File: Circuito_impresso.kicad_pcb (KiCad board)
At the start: 2 copper layers, 78.7 x 62.2 mm, 14 parts, among them J1 Extra_inputs, J2 MAX485M/left, J3 MAX485M/right, J4 RPI, Q1 TIP2955, U1 L7805

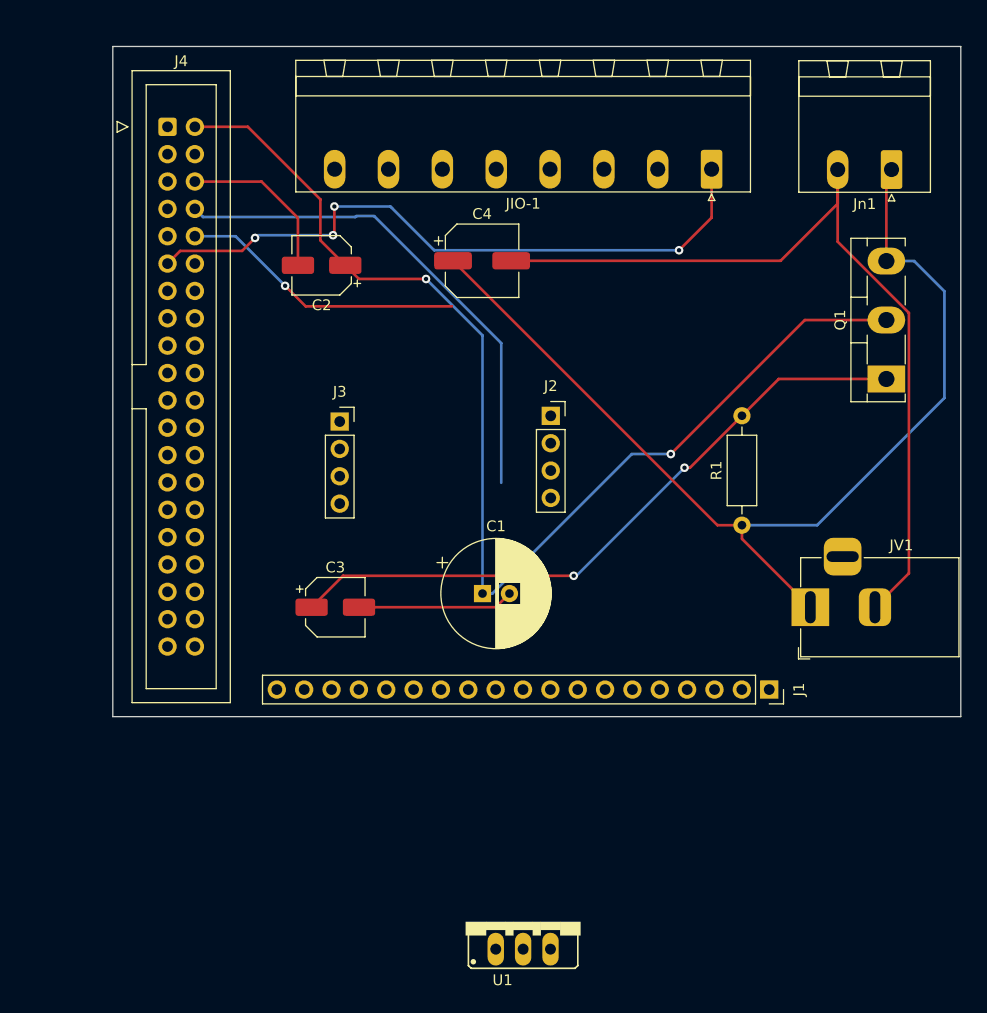
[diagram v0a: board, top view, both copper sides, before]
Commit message: Finalizes the preliminary design of the PCB
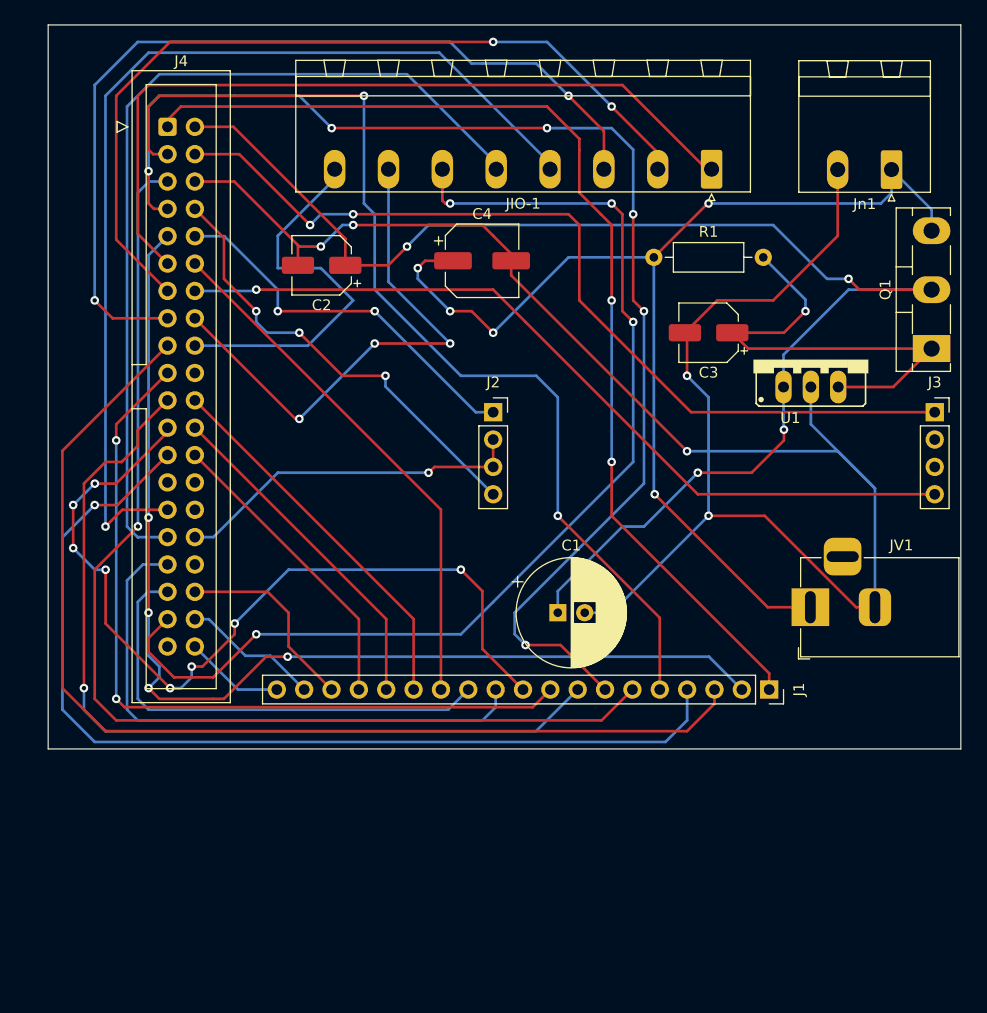
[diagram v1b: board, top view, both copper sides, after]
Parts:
- moved U1 58.6 mm to (171.5, 87.5)
- moved J3 55.3 mm to (183.0, 92.4)
- moved C3 43.0 mm to (162.0, 85.0), turned to 180 degrees
- moved R1 26.2 mm to (156.9, 78.0), turned to 0 degrees
- moved C1 7.21 mm to (148.0, 111.0)
- moved J2 5.36 mm to (142.0, 92.4)
- moved Q1 5.06 mm to (182.7, 86.5)
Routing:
- net Net-(J1-Pad7): track 0.00 -> 119.4 mm, vias 0 -> 6
- net Net-(J1-Pad6): track 0.00 -> 103.8 mm, vias 0 -> 1
- net Net-(J1-Pad2): track 0.00 -> 101.9 mm, vias 0 -> 4
- net Net-(J4-Pad37): track 0.00 -> 101.6 mm, vias 0 -> 4
- net Net-(J1-Pad3): track 0.00 -> 100.4 mm
- net Net-(J1-Pad1): track 0.00 -> 99.1 mm, vias 0 -> 2
- net Net-(J1-Pad5): track 0.00 -> 97.0 mm, vias 0 -> 2
- net Net-(J4-Pad29): track 0.00 -> 94.1 mm, vias 0 -> 1
- net Net-(J1-Pad4): track 0.00 -> 91.9 mm, vias 0 -> 1
- net Net-(J3-Pad1): track 0.00 -> 83.6 mm, vias 0 -> 2
- net Net-(J4-Pad15): track 0.00 -> 83.4 mm, vias 0 -> 2
- net Net-(J4-Pad31): track 0.00 -> 82.7 mm
- net Net-(J1-Pad8): track 0.00 -> 81.1 mm, vias 0 -> 1
- net Net-(J1-Pad10): track 0.00 -> 79.5 mm, vias 0 -> 8
- net Net-(J4-Pad13): track 0.00 -> 78.2 mm, vias 0 -> 2
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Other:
- board size 78.7 x 62.2 mm -> 84.7 x 67.2 mm

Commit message: updates to meet requirements; error correction
the width of the tracks is now 0.8 mm (considering the maximum circuit current of 5 amps, with a maximum increase of 40°C; the position of each terminal of the l7805 in the schematic has been corrected; the position of the L7 so that it heatsink does not collide with the TIP

The silkscreen must be done
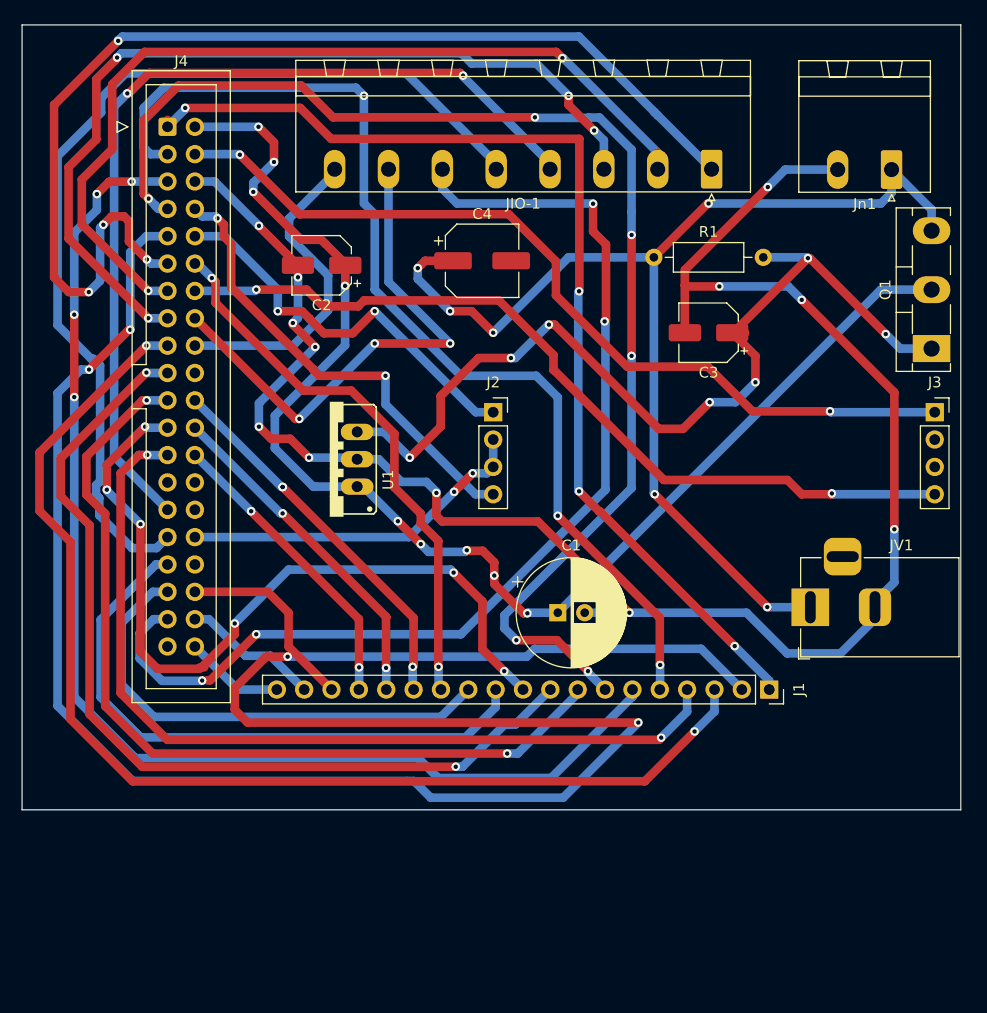
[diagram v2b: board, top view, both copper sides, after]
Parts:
- moved U1 45.6 mm to (126.8, 96.7), turned to 90 degrees
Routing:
- net Net-(J1-Pad2): track 101.9 -> 200.0 mm
- net Net-(C3-Pad1): track 43.5 -> 86.3 mm, vias 1 -> 7
- net Net-(J4-Pad11): track 73.7 -> 105.6 mm, vias 0 -> 4
- net Net-(J1-Pad9): track 73.5 -> 85.9 mm
- net Net-(J1-Pad6): track 103.8 -> 114.0 mm, vias 1 -> 4
- net Net-(J4-Pad31): track 82.7 -> 92.1 mm
- net Net-(J1-Pad4): track 91.9 -> 83.0 mm, vias 1 -> 2
- net Net-(J4-Pad29): track 94.1 -> 85.3 mm, vias 1 -> 2
- net Net-(J1-Pad3): track 100.4 -> 108.9 mm, vias 0 -> 2
- net Net-(C1-Pad1): track 132.2 -> 125.6 mm, vias 4 -> 9
- net Net-(J4-Pad18): track 36.1 -> 30.1 mm
- net Net-(C1-Pad2): track 178.7 -> 172.9 mm, vias 5 -> 12
- net Net-(J1-Pad10): track 79.5 -> 74.1 mm, vias 8 -> 6
- net Net-(J4-Pad13): track 78.2 -> 83.5 mm
- net Net-(J1-Pad11): track 53.2 -> 56.6 mm
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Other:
- board size 84.7 x 67.2 mm -> 87.2 x 72.9 mm

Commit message: Error correction; silkscreen insertion.
The L7805 terminals were inverted on the PCB and have been fixed in this version;

The identification of some of the terminals was made by inserting the serigraphy of the board
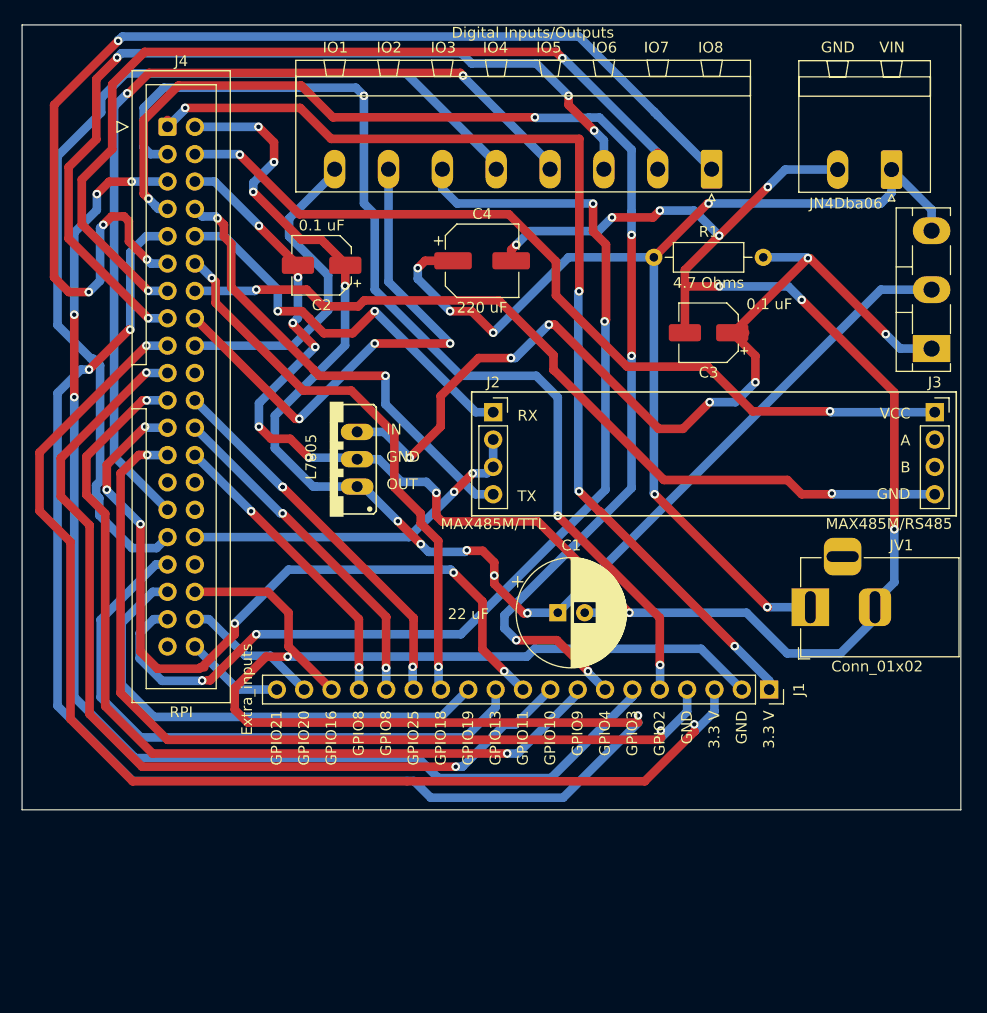
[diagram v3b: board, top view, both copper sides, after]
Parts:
- J2: value MAX485M/left -> MAX485M/TTL
- J3: value MAX485M/right -> MAX485M/RS485
- JIO-1: value Conn_01x08 -> Digital Inputs/Outputs
- renumbered Jn1 to JN4Dba06
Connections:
- U1 pad 1: Net-(C1-Pad1) -> Net-(C3-Pad1)
- U1 pad 3: Net-(C3-Pad1) -> Net-(C1-Pad1)
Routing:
- net Net-(C1-Pad2): track 172.9 -> 195.7 mm, vias 12 -> 16
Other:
- board text added: "3.3 V"
- board text added: "A"
- board text added: "B"
- board text added: "GND"
- board text added: "GPIO10"
- board text added: "GPIO11"
- board text added: "GPIO13"
- board text added: "GPIO16"
- board text added: "GPIO18"
- board text added: "GPIO19"
- board text added: "GPIO2"
- board text added: "GPIO20"
- board text added: "GPIO21"
- board text added: "GPIO25"
- board text added: "GPIO3"
- board text added: "GPIO4"
- board text added: "GPIO8"
- board text added: "GPIO9"
- board text added: "IN"
- board text added: "IO1"
- board text added: "IO2"
- board text added: "IO3"
- board text added: "IO4"
- board text added: "IO5"
- board text added: "IO6"
- board text added: "IO7"
- board text added: "IO8"
- board text added: "OUT"
- board text added: "RX"
- board text added: "TX"
- board text added: "VCC"
- board text added: "VIN"

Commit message: Adjustments
Capacitors C2 and C3 have been upgraded from SMD to not polarized through hole; the radius of C1 has been updated; inserted pcb version.
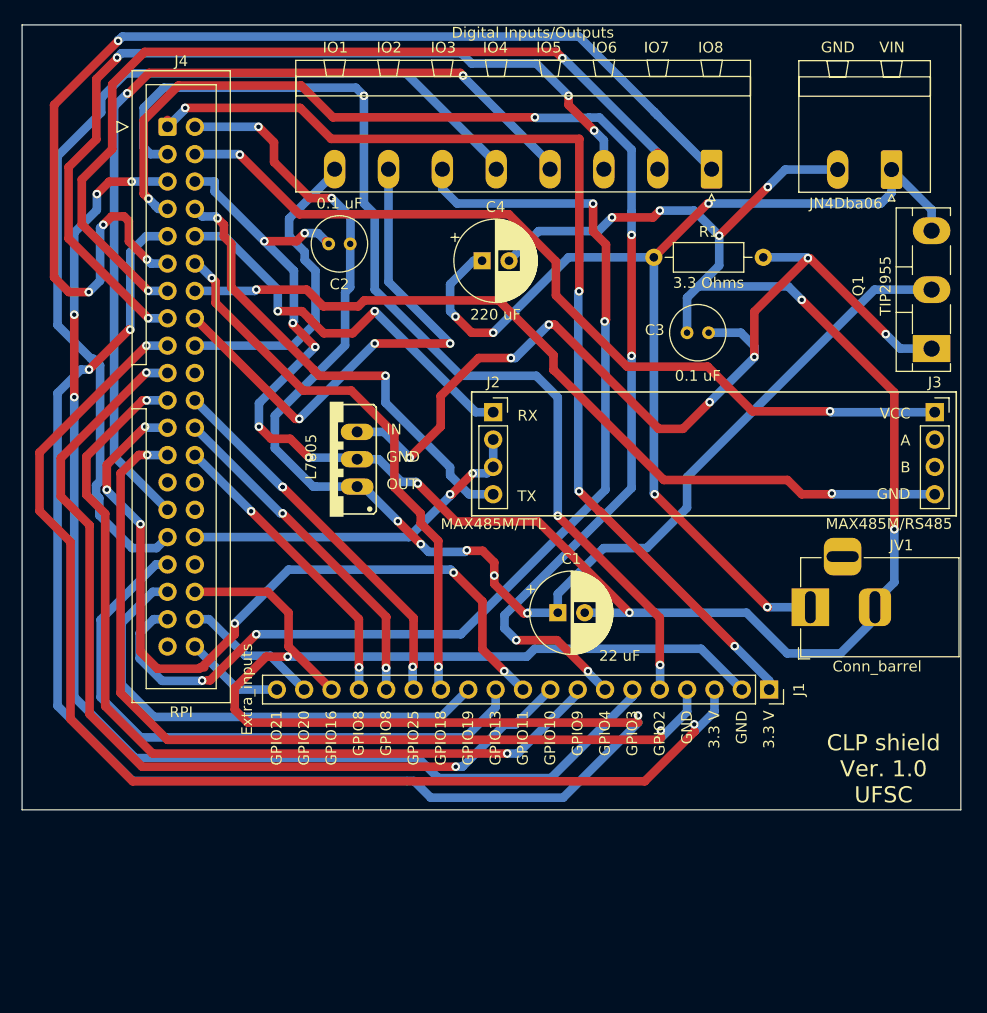
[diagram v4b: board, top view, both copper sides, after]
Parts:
- C1: footprint Capacitor_THT:CP_Radial_D10.0mm_P2.50mm -> Capacitor_THT:CP_Radial_D7.5mm_P2.50mm
- C2, C3: footprint Capacitor_SMD:CP_Elec_5x3 -> Capacitor_THT:C_Radial_D5.0mm_H5.0mm_P2.00mm
- C4: footprint Capacitor_SMD:CP_Elec_6.3x7.7 -> Capacitor_THT:CP_Radial_D7.5mm_P2.50mm
- JV1: value Conn_01x02 -> Conn_barrel
- R1: value 4.7 Ohms -> 3.3 Ohms
- moved C2 3.32 mm to (128.7, 76.8)
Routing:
- net Net-(C1-Pad2): track 195.7 -> 199.4 mm, vias 16 -> 14
- net Net-(C4-Pad1): track 106.3 -> 103.9 mm, vias 6 -> 5
- net Net-(C1-Pad1): track 125.6 -> 127.1 mm, vias 9 -> 7
- net Net-(C3-Pad1): track 86.3 -> 87.6 mm
- net Net-(J4-Pad18): track 30.1 -> 29.1 mm
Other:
- board text added: "CLP shield Ver. 1.0 UFSC"
